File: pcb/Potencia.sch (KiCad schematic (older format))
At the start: 58 parts, among them U4 L298P, U5 L298P

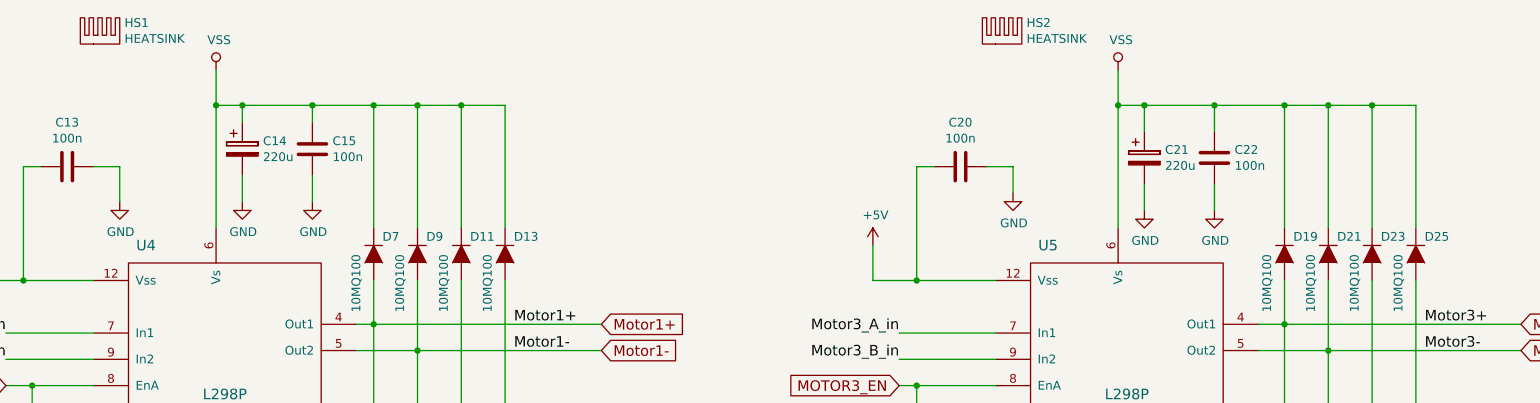
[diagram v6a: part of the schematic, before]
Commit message: finalizado el posicionado sobre la pcb
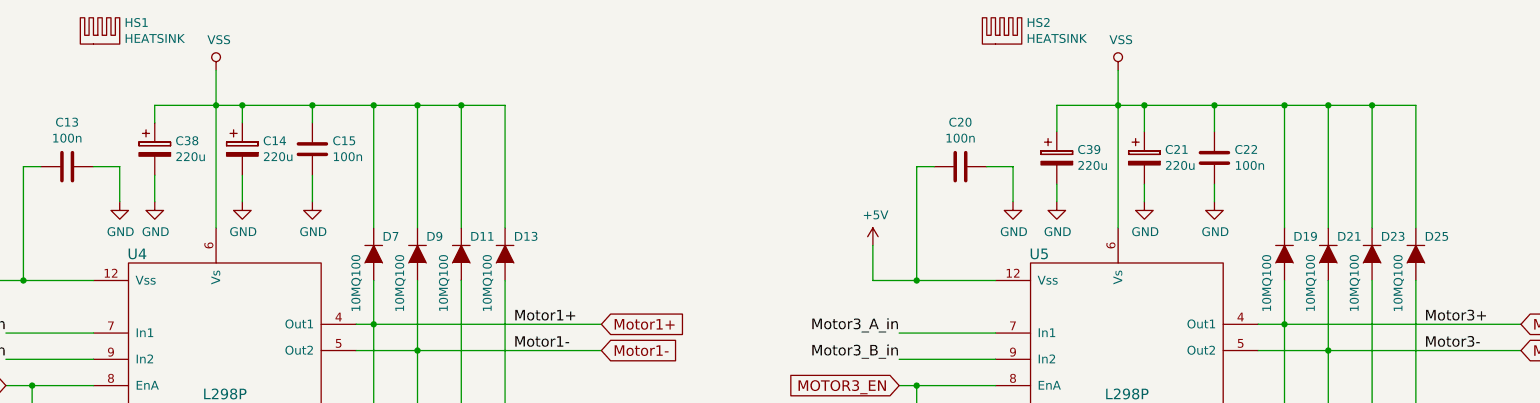
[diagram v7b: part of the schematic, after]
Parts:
- added C38, C39: 220u, Capacitors_SMD:c_elec_10x10, symbol CP
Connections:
- net GND: now also C38.2, C39.2
- net VSS: now also C38.1, C39.1
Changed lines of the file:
@@
 L GND #PWR020
 U 1 1 5769AEAD
-P 8550 1750
-F 0 "#PWR020" H 8550 1500 50  0001 C CNN
-F 1 "GND" H 8555 1577 50  0000 C CNN
-F 2 "" H 8550 1750 50  0000 C CNN
-F 3 "" H 8550 1750 50  0000 C CNN
-	1    8550 1750
+P 8550 1700
+F 0 "#PWR020" H 8550 1450 50  0001 C CNN
+F 1 "GND" H 8555 1527 50  0000 C CNN
+F 2 "" H 8550 1700 50  0000 C CNN
+F 3 "" H 8550 1700 50  0000 C CNN
+	1    8550 1700
 	1    0    0    -1
 $EndComp
@@
 L GND #PWR021
 U 1 1 5769B207
-P 7400 1650
-F 0 "#PWR021" H 7400 1400 50  0001 C CNN
-F 1 "GND" H 7405 1477 50  0000 C CNN
-F 2 "" H 7400 1650 50  0000 C CNN
-F 3 "" H 7400 1650 50  0000 C CNN
-	1    7400 1650
+P 7400 1700
+F 0 "#PWR021" H 7400 1450 50  0001 C CNN
+F 1 "GND" H 7405 1527 50  0000 C CNN
+F 2 "" H 7400 1700 50  0000 C CNN
+F 3 "" H 7400 1700 50  0000 C CNN
+	1    7400 1700
 	1    0    0    -1
 $EndComp
@@
 L GND #PWR034
 U 1 1 5769F9F7
-P 8150 1750
-F 0 "#PWR034" H 8150 1500 50  0001 C CNN
-F 1 "GND" H 8155 1577 50  0000 C CNN
-F 2 "" H 8150 1750 50  0000 C CNN
-F 3 "" H 8150 1750 50  0000 C CNN
-	1    8150 1750
+P 8150 1700
+F 0 "#PWR034" H 8150 1450 50  0001 C CNN
+F 1 "GND" H 8155 1527 50  0000 C CNN
+F 2 "" H 8150 1700 50  0000 C CNN
+F 3 "" H 8150 1700 50  0000 C CNN
+	1    8150 1700
 	1    0    0    -1
 $EndComp
@@
 	3400 1550 3400 1700
 Wire Wire Line
-	8550 1600 8550 1750
+	8550 1600 8550 1700
 Wire Wire Line
 	8550 1150 8550 1300
 Wire Wire Line
-	8000 1150 9700 1150
+	7650 1150 9700 1150
 Wire Wire Line
 	8000 950  8000 1850
@@
 	2300 1500 2150 1500
 Wire Wire Line
-	7400 1650 7400 1500
+	7400 1700 7400 1500
 Wire Wire Line
 	7400 1500 7250 1500
@@
 Connection ~ 3400 1150
 Wire Wire Line
-	3000 1250 3000 1150
+	3000 1150 3000 1250
 Connection ~ 3000 1150
 Wire Wire Line
-	2850 1150 4500 1150
+	2500 1150 4500 1150
 Wire Wire Line
 	4250 1150 4250 1850
@@
 Connection ~ 9700 3100
 Wire Wire Line
-	8150 1750 8150 1600
+	8150 1700 8150 1600
 Wire Wire Line
 	8150 1300 8150 1150
@@
 U 1 1 5771BE9E
 P 2350 3650
-F 0 "U4" H 2450 5350 60  0000 C CNN
+F 0 "U4" H 2400 5300 60  0000 C CNN
 F 1 "L298P" H 2900 4500 60  0000 C CNN
 F 2 "MotorDrivers:L298_PowerSO20" H 2350 3650 60  0001 C CNN
@@
 U 1 1 5771C16D
 P 7500 3650
-F 0 "U5" H 7600 5350 60  0000 C CNN
+F 0 "U5" H 7550 5300 60  0000 C CNN
 F 1 "L298P" H 8050 4500 60  0000 C CNN
 F 2 "MotorDrivers:L298_PowerSO20" H 7500 3650 60  0001 C CNN
@@
 	1    0    0    -1
 $EndComp
+$Comp
+L CP C38
+U 1 1 578EB723
+P 2500 1400
+F 0 "C38" H 2618 1446 50  0000 L CNN
+F 1 "220u" H 2618 1355 50  0000 L CNN
+F 2 "Capacitors_SMD:c_elec_10x10" H 2538 1250 50  0001 C CNN
+F 3 "" H 2500 1400 50  0000 C CNN
+F 4 "PANASONIC" H 2500 1400 60  0001 C CNN "Fabricante"
+F 5 "SC1H227M10010VR" H 2500 1400 60  0001 C CNN "Ref"
+F 6 "~" H 2500 1400 60  0001 C CNN "Potencia"
+F 7 "~" H 2500 1400 60  0001 C CNN "Tolerancia"
+F 8 "tme" H 2500 1400 60  0001 C CNN "Provedor"
+F 9 "SC1H227M10010VR" H 2500 1400 60  0001 C CNN "Ref_Proveedor"
+	1    2500 1400
+	1    0    0    -1
+$EndComp
+Wire Wire Line
+	2500 1250 2500 1150
+$Comp
+L GND #PWR046
+U 1 1 578EB927
+P 2500 1700
+F 0 "#PWR046" H 2500 1450 50  0001 C CNN
+F 1 "GND" H 2505 1527 50  0000 C CNN
+F 2 "" H 2500 1700 50  0000 C CNN
+F 3 "" H 2500 1700 50  0000 C CNN
+	1    2500 1700
+	1    0    0    -1
+$EndComp
+Wire Wire Line
+	2500 1700 2500 1550
+$Comp
+L CP C39
+U 1 1 578EBCE1
+P 7650 1450
+F 0 "C39" H 7768 1496 50  0000 L CNN
+F 1 "220u" H 7768 1405 50  0000 L CNN
+F 2 "Capacitors_SMD:c_elec_10x10" H 7688 1300 50  0001 C CNN
+F 3 "" H 7650 1450 50  0000 C CNN
+F 4 "SAMWHA" H 7650 1450 60  0001 C CNN "Fabricante"
+F 5 "SC1H227M10010VR" H 7650 1450 60  0001 C CNN "Ref"
+F 6 "~" H 7650 1450 60  0001 C CNN "Potencia"
+F 7 "~" H 7650 1450 60  0001 C CNN "Tolerancia"
+F 8 "tme" H 7650 1450 60  0001 C CNN "Provedor"
+F 9 "SC1H227M10010VR" H 7650 1450 60  0001 C CNN "Ref_Proveedor"
+	1    7650 1450
+	1    0    0    -1
+$EndComp
+Wire Wire Line
+	7650 1300 7650 1150
+$Comp
+L GND #PWR047
+U 1 1 578EBEC4
+P 7650 1700
+F 0 "#PWR047" H 7650 1450 50  0001 C CNN
+F 1 "GND" H 7655 1527 50  0000 C CNN
+F 2 "" H 7650 1700 50  0000 C CNN
+F 3 "" H 7650 1700 50  0000 C CNN
+	1    7650 1700
+	1    0    0    -1
+$EndComp
+Wire Wire Line
+	7650 1700 7650 1600
 $EndSCHEMATC
